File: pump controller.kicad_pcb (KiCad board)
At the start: 2 copper layers, 200 x 150 mm, 86 parts, among them J1 Button Terminal, J10 I2C Header 1, J2 Power Terminal, J3 Water Sensor Connector, J4 Motor Connector, J5 I2C Header 2, J6 Digital Connector, J7 Motor Connector, M3 MountingHole_3.2mm_M3_Pad_Via, M5 MountingHole_5mm, M5 MountingHole_5x9mm, Q1 AZ7033Z-E1, Q10 VNP5N07, Q2 2N3904, Q3 2N3904, Q4 2N3904, Q5 2N3904, Q6 2N3904, Q7 2N3904, Q8 2N3904, Q9 2N3904, U1 WeMos_mini, U2 TC4422, U3 12V8A_5V1A_supply

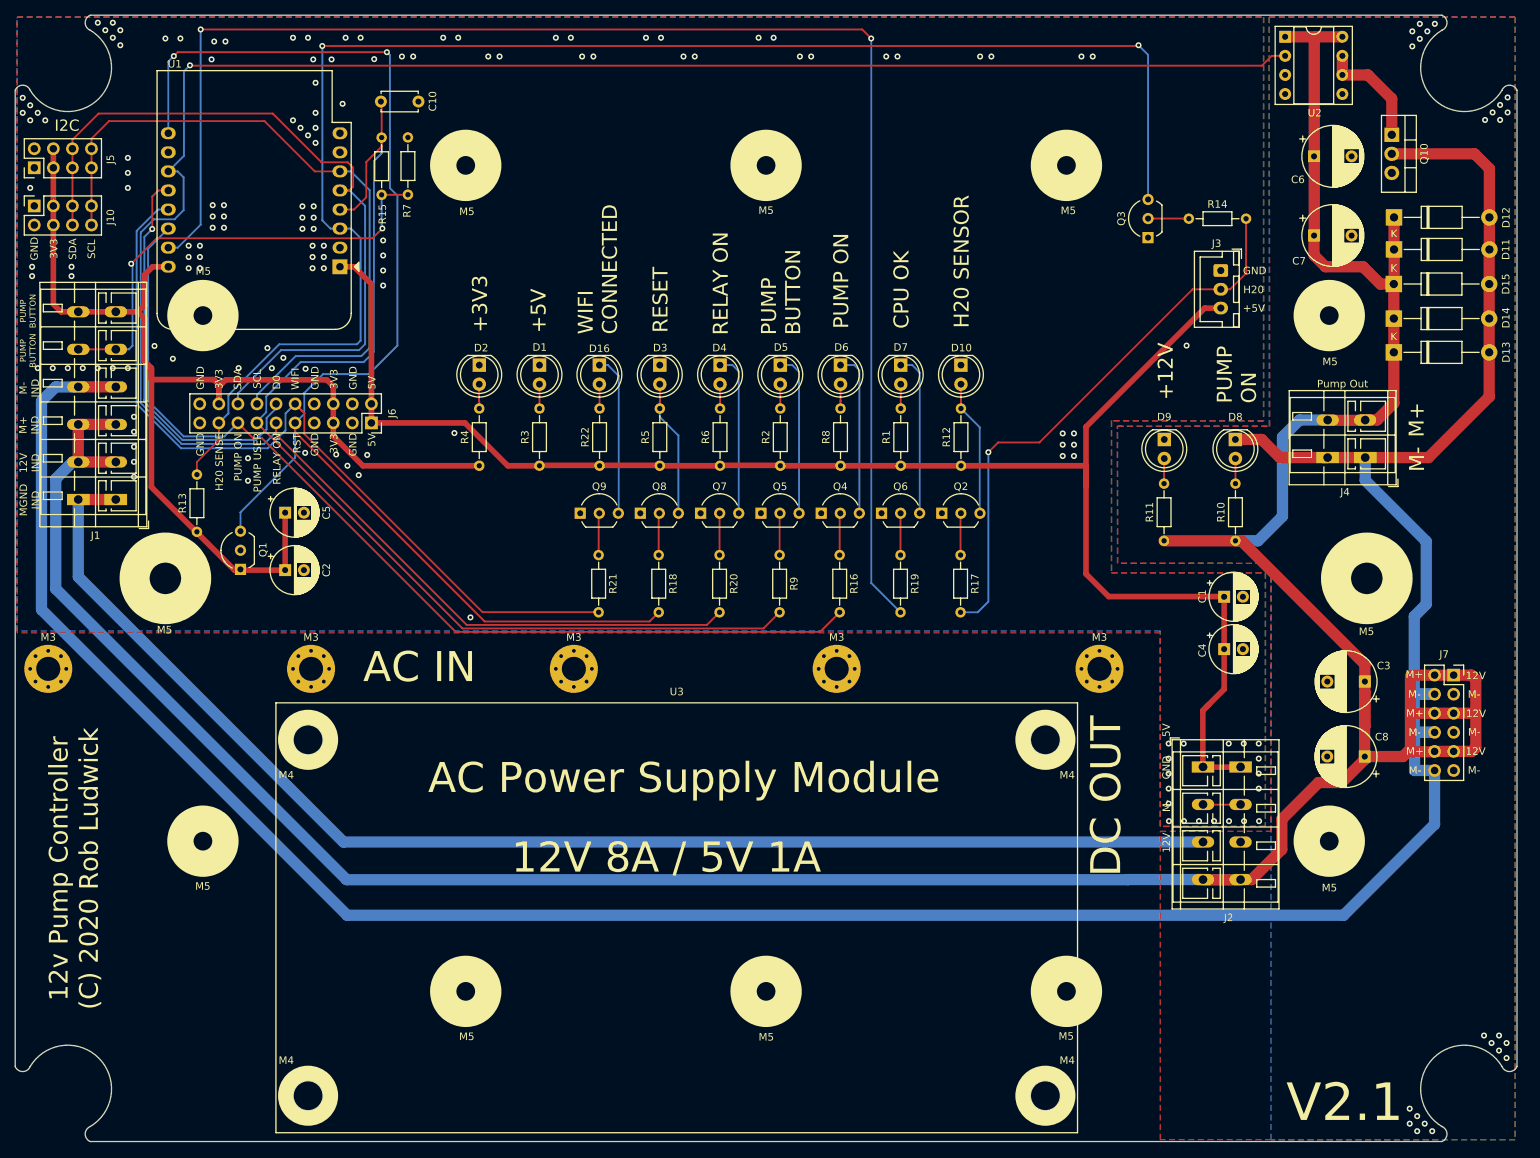
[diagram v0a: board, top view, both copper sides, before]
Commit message: Added a zener diode in front of the capacitors on the 5v rail
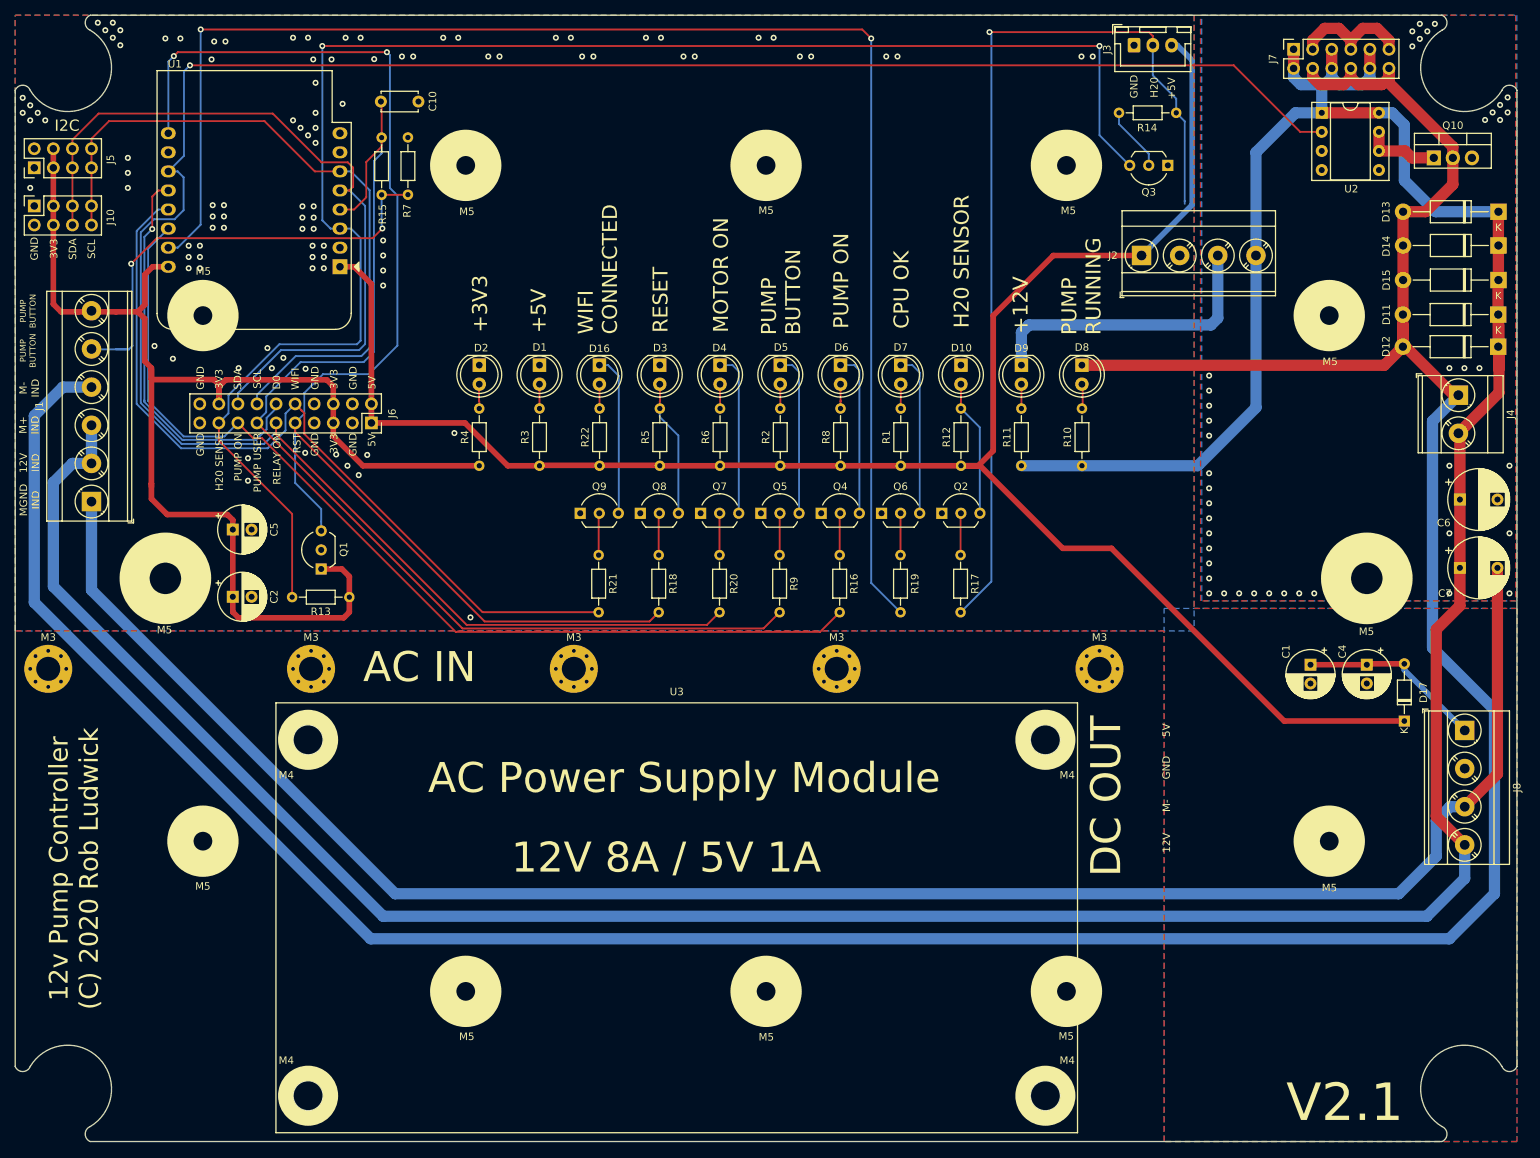
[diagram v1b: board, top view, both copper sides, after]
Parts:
- removed C3, C8: 1000uF, Capacitor_THT:CP_Radial_D8.0mm_P5.00mm
- added D17: D_Schottky, Diode_THT:D_DO-34_SOD68_P7.62mm_Horizontal, F.Cu at (215.0, 107.0)
- added J8: Power In Terminal, TerminalBlock_Phoenix:TerminalBlock_Phoenix_MKDS-3-4-5.08_1x04_P5.08mm_Horizontal, F.Cu at (223.0, 108.2)
- J1: footprint TerminalBlock_WAGO:TerminalBlock_WAGO_236-406_1x06_P5.00mm_45Degree -> TerminalBlock_Phoenix:TerminalBlock_Phoenix_MKDS-3-6-5.08_1x06_P5.08mm_Horizontal
- J2: value Power Terminal -> Power Out Terminal; footprint TerminalBlock_WAGO:TerminalBlock_WAGO_236-404_1x04_P5.00mm_45Degree -> TerminalBlock_Phoenix:TerminalBlock_Phoenix_MKDS-3-4-5.08_1x04_P5.08mm_Horizontal
- J4: footprint TerminalBlock_WAGO:TerminalBlock_WAGO_236-402_1x02_P5.00mm_45Degree -> TerminalBlock_Phoenix:TerminalBlock_Phoenix_MKDS-3-2-5.08_1x02_P5.08mm_Horizontal
- moved J7 86.0 mm to (200.2, 17.5), turned to 90 degrees
- moved J2 69.4 mm to (180.0, 45.0), turned to 0 degrees
- moved C6 49.7 mm to (222.4, 77.5)
- moved C7 48.3 mm to (222.4, 86.6)
- moved J3 32.1 mm to (179.0, 17.0), turned to 0 degrees
- moved D13 23.3 mm to (227.5, 39.2), turned to 180 degrees
- moved R10 22.8 mm to (172.1, 73.0)
- moved D8 22.7 mm to (172.1, 59.6)
- moved D12 22.1 mm to (227.5, 57.1), turned to 180 degrees
- moved R13 22.1 mm to (74.5, 90.5), turned to 180 degrees
- moved R11 21.5 mm to (164.0, 73.0)
- moved D9 21.4 mm to (164.0, 59.6)
- moved J4 19.3 mm to (222.2, 63.6), turned to 270 degrees
- moved C4 19.1 mm to (210.0, 99.5), turned to 270 degrees
- moved D14 17.0 mm to (227.5, 43.7), turned to 180 degrees
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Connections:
- C1 pad 1: +5V -> +5VIN
- C4 pad 1: +5V -> +5VIN
- U1 pad 10: (no net) -> Net-(U1-Pad10)
- U1 pad 7: (no net) -> Net-(U1-Pad7)
- U1 pad 8: (no net) -> Net-(U1-Pad8)
- U2 pad 3: (no net) -> Net-(U2-Pad3)
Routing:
- net MOTOR_GND: track 179.7 -> 308.6 mm, vias 24 -> 42
- net SENSOR_OUT: track 75.7 -> 125.1 mm
- net MOTOR-: track 394.4 -> 437.8 mm
- net +5V: track 217.6 -> 256.3 mm
- net +5VIN: track 0.00 -> 25.1 mm
- net +3V3: track 153.7 -> 176.1 mm
- net MOTOR+: track 449.2 -> 471.1 mm
- net WATER_PRESENT: track 205.8 -> 216.1 mm
- net MOTOR_ON: track 292.1 -> 300.1 mm
- net SIGNAL_GND: track 5.08 -> 0.00 mm, vias 144 -> 100
- net /MOS_IN: track 15.2 -> 10.2 mm
- net Net-(Q3-Pad2): track 5.44 -> 8.64 mm
- net RESET: track 176.4 -> 174.9 mm
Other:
- board text added: "MOTOR ON"
- board text added: "PUMP RUNNING"
- board text removed: "M+"
- board text removed: "Pump Out"

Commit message: Updated debug lines.  Added python logo.
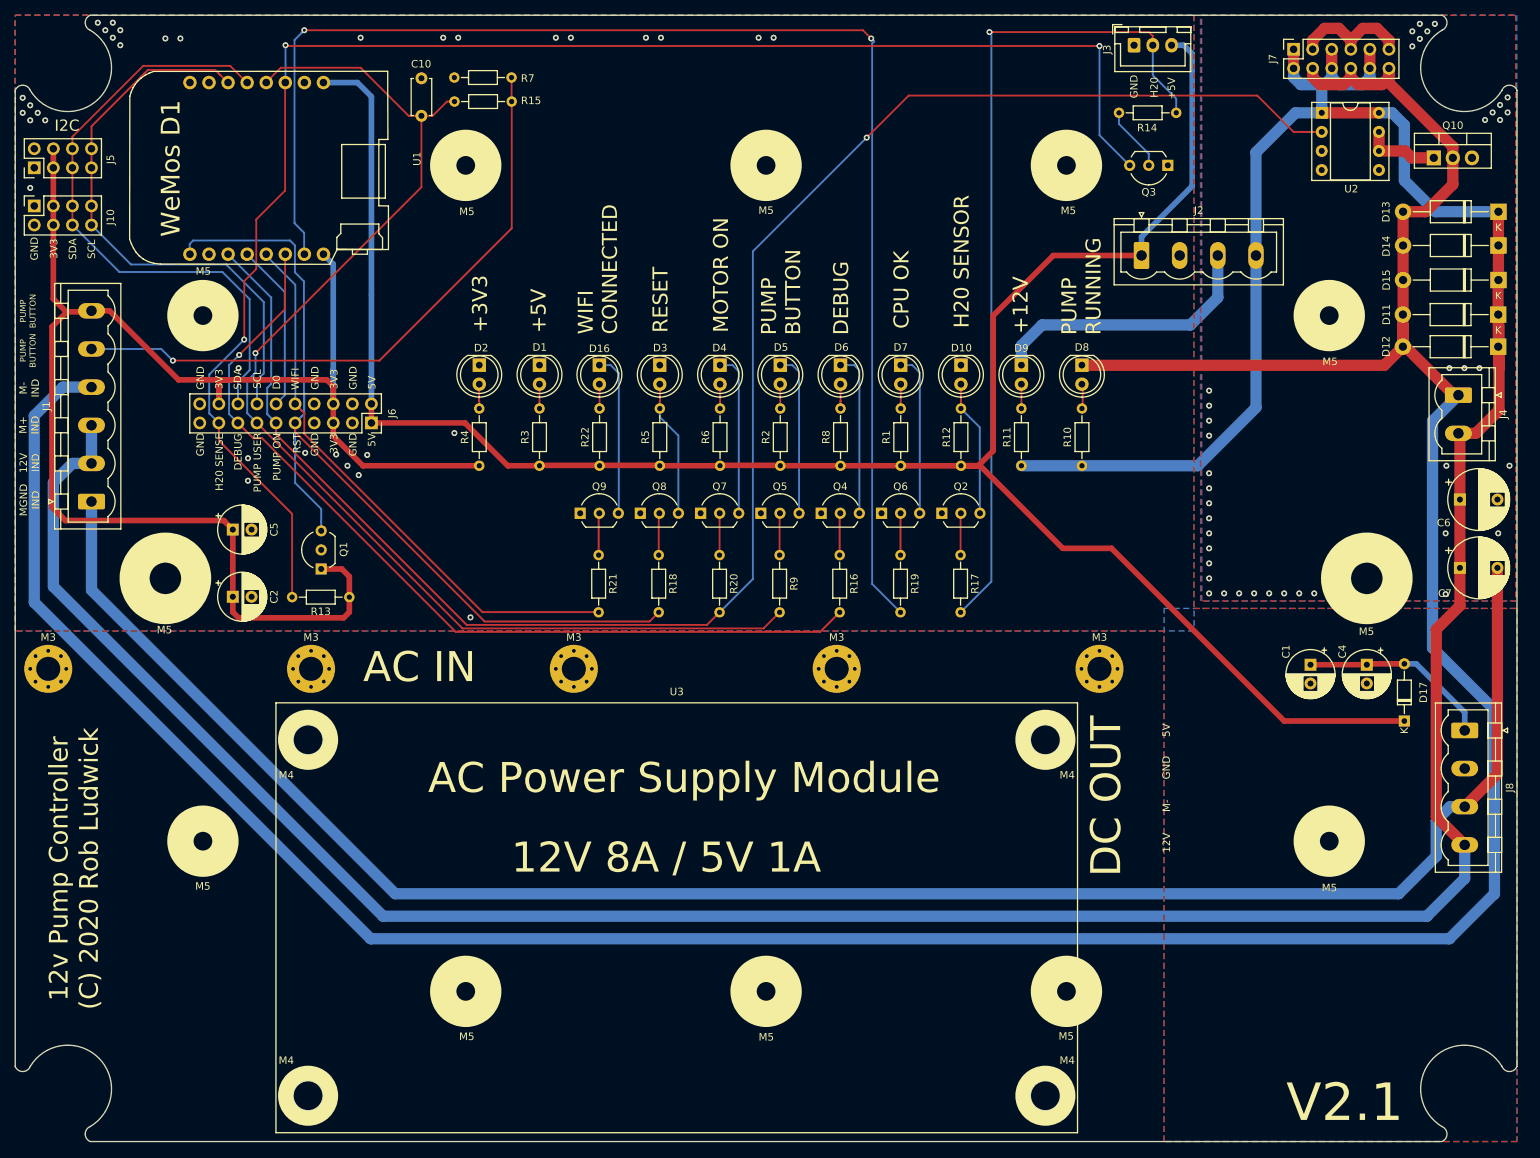
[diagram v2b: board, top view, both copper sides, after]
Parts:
- J1: footprint TerminalBlock_Phoenix:TerminalBlock_Phoenix_MKDS-3-6-5.08_1x06_P5.08mm_Horizontal -> Connector_Phoenix_MSTB:PhoenixContact_MSTBVA_2,5_6-G-5,08_1x06_P5.08mm_Vertical
- J2, J8: footprint TerminalBlock_Phoenix:TerminalBlock_Phoenix_MKDS-3-4-5.08_1x04_P5.08mm_Horizontal -> Connector_Phoenix_MSTB:PhoenixContact_MSTBVA_2,5_4-G-5,08_1x04_P5.08mm_Vertical
- J4: footprint TerminalBlock_Phoenix:TerminalBlock_Phoenix_MKDS-3-2-5.08_1x02_P5.08mm_Horizontal -> Connector_Phoenix_MSTB:PhoenixContact_MSTBVA_2,5_2-G-5,08_1x02_P5.08mm_Vertical
- U1: footprint Module:WEMOS_D1_mini_light -> pump-controller:D1_mini_board
- moved R7 20.8 mm to (96.1, 21.3), turned to 180 degrees
- moved U1 15.6 mm to (64.7, 33.4), turned to 90 degrees
- moved R15 10.8 mm to (88.5, 24.5), turned to 0 degrees
- moved C10 5.72 mm to (84.1, 26.4), turned to 90 degrees
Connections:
- net PUMP_IND renamed DEBUG
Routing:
- net MOTOR_ON: track 300.1 -> 236.5 mm
- net RESET: track 174.9 -> 121.6 mm, vias 2 -> 0
- net WIFI: track 109.3 -> 75.1 mm
- net PIN_D5: track 53.3 -> 23.1 mm, vias 1 -> 0
- net +3V3: track 176.1 -> 204.4 mm
- net +5V: track 256.3 -> 283.8 mm
- net PUMP_BUTTON: track 61.9 -> 84.1 mm, vias 2 -> 1
- net SDA: track 101.3 -> 82.6 mm
- net SCL: track 93.1 -> 77.8 mm
- net CPU_OK: track 199.4 -> 185.1 mm
- net PUMP_USER_SIG: track 149.4 -> 162.4 mm, vias 0 -> 1
- net DEBUG: track 131.5 -> 118.8 mm, vias 0 -> 1
- net SENSOR_OUT: track 125.1 -> 112.6 mm
- net WATER_PRESENT: track 216.1 -> 208.3 mm, vias 2 -> 3
- net MOTOR_GND: track 308.6 -> 305.9 mm, vias 42 -> 40
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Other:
- board text added: "DEBUG"
- board text removed: "RELAY ON"

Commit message: Added python logo.
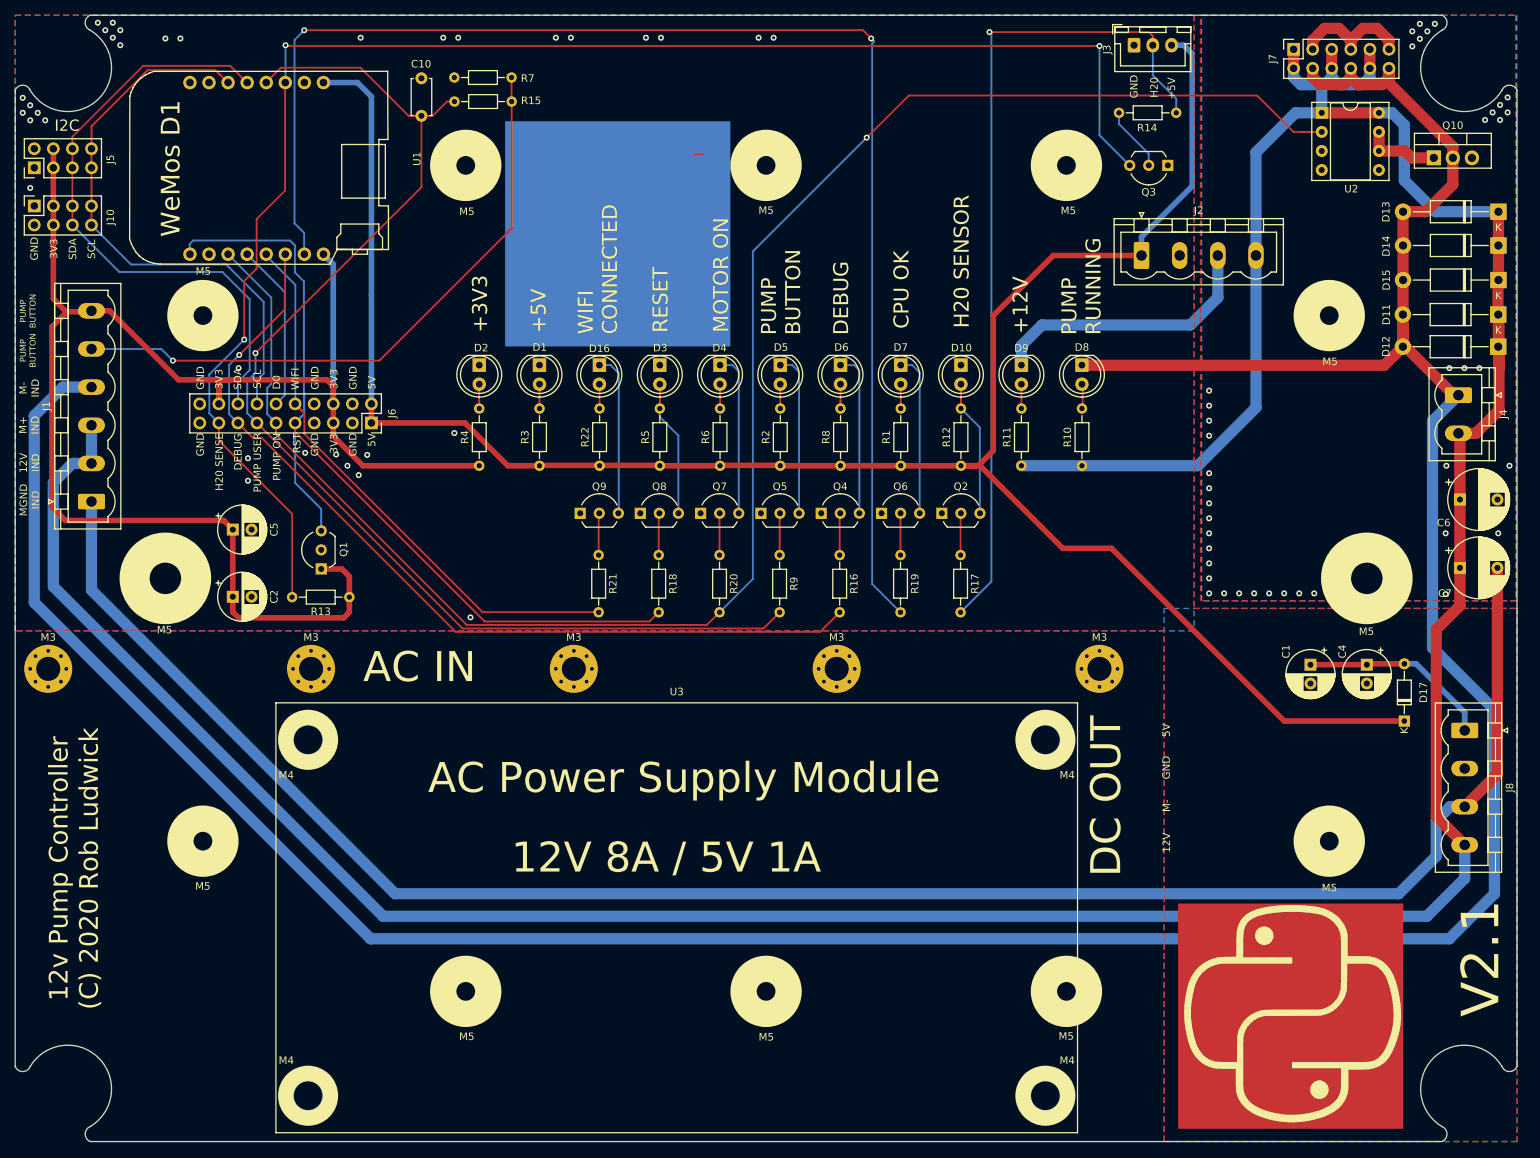
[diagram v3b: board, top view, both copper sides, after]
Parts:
- added Ref**: Val**, pump-controller:pythonlogo, B.Cu at (110.2, 42.1)
- added Ref**: Val**, pump-controller:pythonlogo, F.Cu at (199.8, 146.3)
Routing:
- net (no net): track 0.00 -> 1.40 mm
